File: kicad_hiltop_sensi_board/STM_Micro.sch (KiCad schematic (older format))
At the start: 21 parts, among them SW1 SW_Push, U22 STM32F072RBTx, Y2 8MHZ, Y3 ABS25-32.768KHZ-6-T

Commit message: revb design updated schematics and layout
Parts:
- added C84: 100nF, Capacitor_SMD:C_0402_1005Metric, symbol device:C
- added J9: Conn_02x05_Odd_Even, Connector_PinHeader_2.54mm:PinHeader_2x05_P2.54mm_Vertical, symbol Connector:Conn_02x05_Odd_Even
- added R163: DNF, Resistor_SMD:R_0603_1608Metric, symbol Sensi_Board-rescue:R-device
- added R164: DNF, Resistor_SMD:R_0402_1005Metric, symbol device:R
- added R39, R40: 100k, Capacitor_SMD:C_0603_1608Metric, symbol device:R
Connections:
- net GPIO5 is gone; now on net SB1: U22.33 (I2S2_WS/SPI2_NSS/TIM15_BKIN/TIM1_BKIN/TSC_G6_IO2/USART3_CK/PB12)
- net +3V3: now also C84.2, J9.1 (Pin_1), R39.1
- net ADC7: now also U22.21 (ADC_IN5/CEC/COMP1_INM/COMP2_INM/DAC_OUT2/I2S1_CK/SPI1_SCK/TIM2_CH1/TIM2_ETR/TSC_G2_IO2/PA5); no longer U22.27 (ADC_IN9/TIM14_CH1/TIM1_CH3N/TIM3_CH4/TSC_G3_IO3/USART3_DE/USART3_RTS/PB1)
- net BOOT0: now also R163.1
- net GND: now also C84.1, J9.3 (Pin_3), J9.5 (Pin_5), J9.9 (Pin_9), R163.2, R164.2, R40.1; no longer U22.18 (VSS)
- net NRST: now also J9.10 (Pin_10)
- net SB1: no longer U22.2 (PC13/RTC_OUT_ALARM/RTC_OUT_CALIB/RTC_TAMP1/RTC_TS/SYS_WKUP2)
- net SWD_IO: now also J9.2 (Pin_2), R39.2
- net SWD_SCK: now also J9.4 (Pin_4), R40.2
- net at R124.2: now also U22.27 (ADC_IN9/TIM14_CH1/TIM1_CH3N/TIM3_CH4/TSC_G3_IO3/USART3_DE/USART3_RTS/PB1); no longer U22.21 (ADC_IN5/CEC/COMP1_INM/COMP2_INM/DAC_OUT2/I2S1_CK/SPI1_SCK/TIM2_CH1/TIM2_ETR/TSC_G2_IO2/PA5)
- new net: R164.1, U22.18 (VSS)
- no-connect marks 3 -> 7
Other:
- note added: "JTAG Header\n"
- note added: "Note: only for stm32f072 fit 0R to gnd. for 303/302 model DNF\n"
- moved on the sheet: D13, R124

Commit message: revB ready for review
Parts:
- added J10: Conn_01x04, Connector_PinHeader_1.27mm:PinHeader_1x04_P1.27mm_Vertical, symbol Connector:Conn_01x04
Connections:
- net +3V3: now also J10.1 (Pin_1)
- net DEBUG_UART_RX: now also J10.2 (Pin_2)
- net DEBUG_UART_TX: now also J10.3 (Pin_3)
- net GND: now also J10.4 (Pin_4)
- net SB1 renamed GPIO5
- net SB2 renamed GPIO6
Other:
- note added: "Serial Debug Header\n"
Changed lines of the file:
@@
 STM_RES1
 Text HLabel 11800 3175 2    60   BiDi ~ 0
-SB2
+GPIO6
 Text HLabel 11775 6075 2    60   BiDi ~ 0
 RTD3_INT
 Text HLabel 11775 5975 2    60   BiDi ~ 0
-SB1
+GPIO5
 Text HLabel 11800 4575 2    60   BiDi ~ 0
 GPIO1
@@
 Text Label 4350 3075 2    60   ~ 0
 STM_RESET
+Text Notes 10350 7500 0    118  ~ 24
+Serial Debug Header\n
+Wire Notes Line
+	9950 9225 12575 9225
+Wire Notes Line
+	12575 9225 12575 7250
+Wire Notes Line
+	12575 7250 9950 7250
+Wire Notes Line
+	9950 7250 9950 9225
+$Comp
+L Connector:Conn_01x04 J10
+U 1 1 602D0955
+P 11425 8250
+F 0 "J10" H 11505 8242 50  0000 L CNN
+F 1 "Conn_01x04" H 11505 8151 50  0000 L CNN
+F 2 "Connector_PinHeader_1.27mm:PinHeader_1x04_P1.27mm_Vertical" H 11425 8250 50  0001 C CNN
+F 3 "~" H 11425 8250 50  0001 C CNN
+	1    11425 8250
+	1    0    0    -1
+$EndComp
+$Comp
+L power:+3V3 #PWR0264
+U 1 1 602D1336
+P 11125 8075
+F 0 "#PWR0264" H 11125 7925 50  0001 C CNN
+F 1 "+3V3" H 11140 8248 50  0000 C CNN
+F 2 "" H 11125 8075 50  0001 C CNN
+F 3 "" H 11125 8075 50  0001 C CNN
+	1    11125 8075
+	1    0    0    -1
+$EndComp
+Wire Wire Line
+	11225 8150 11125 8150
+Wire Wire Line
+	11125 8150 11125 8075
+Text Label 10825 5775 0    60   ~ 0
+DEBUG_TX
+Text Label 10825 5875 0    60   ~ 0
+DEBUG_RX
+Text Label 10725 8350 0    60   ~ 0
+DEBUG_TX
+Text Label 10725 8250 0    60   ~ 0
+DEBUG_RX
+Wire Wire Line
+	10725 8250 11225 8250
+Wire Wire Line
+	10725 8350 11225 8350
+$Comp
+L power:GND #PWR0265
+U 1 1 60317C84
+P 11150 8550
+F 0 "#PWR0265" H 11150 8300 50  0001 C CNN
+F 1 "GND" H 11155 8377 50  0000 C CNN
+F 2 "" H 11150 8550 50  0001 C CNN
+F 3 "" H 11150 8550 50  0001 C CNN
+	1    11150 8550
+	1    0    0    -1
+$EndComp
+Wire Wire Line
+	11150 8550 11150 8450
+Wire Wire Line
+	11150 8450 11225 8450
 $EndSCHEMATC

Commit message: Sensi Board RevB
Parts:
- added R172: DNF, Resistor_SMD:R_0603_1608Metric, symbol device:R
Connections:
- net +3V3: now also R172.1
- net BOOT0: now also R172.2
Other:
- moved on the sheet: R120
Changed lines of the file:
@@
 L Sensi_Board-rescue:R-device R120
 U 1 1 5F95CC59
-P 2725 2850
-F 0 "R120" H 2795 2896 50  0000 L CNN
-F 1 "10K" H 2795 2805 50  0000 L CNN
-F 2 "Resistor_SMD:R_0603_1608Metric" V 2655 2850 50  0001 C CNN
-F 3 "" H 2725 2850 50  0001 C CNN
-F 4 "101-010" H 0   0   50  0001 C CNN "Devtank"
-	1    2725 2850
-	1    0    0    -1
-$EndComp
-Wire Wire Line
-	2725 3000 2725 3075
-Connection ~ 2725 3075
+P 3250 2850
+F 0 "R120" H 3320 2896 50  0000 L CNN
+F 1 "10K" H 3320 2805 50  0000 L CNN
+F 2 "Resistor_SMD:R_0603_1608Metric" V 3180 2850 50  0001 C CNN
+F 3 "" H 3250 2850 50  0001 C CNN
+F 4 "101-010" H 525 0   50  0001 C CNN "Devtank"
+	1    3250 2850
+	1    0    0    -1
+$EndComp
+Wire Wire Line
+	3250 3000 3250 3075
 $Comp
 L power:+3V3 #PWR0186
 U 1 1 5F95F542
-P 2725 2625
-F 0 "#PWR0186" H 2725 2475 50  0001 C CNN
-F 1 "+3V3" H 2740 2798 50  0000 C CNN
-F 2 "" H 2725 2625 50  0001 C CNN
-F 3 "" H 2725 2625 50  0001 C CNN
-	1    2725 2625
-	1    0    0    -1
-$EndComp
-Wire Wire Line
-	2725 2625 2725 2700
-Wire Wire Line
-	2300 3075 2725 3075
-Text HLabel 2300 3075 0    60   Input ~ 0
+P 3250 2625
+F 0 "#PWR0186" H 3250 2475 50  0001 C CNN
+F 1 "+3V3" H 3265 2798 50  0000 C CNN
+F 2 "" H 3250 2625 50  0001 C CNN
+F 3 "" H 3250 2625 50  0001 C CNN
+	1    3250 2625
+	1    0    0    -1
+$EndComp
+Wire Wire Line
+	3250 2625 3250 2700
+Wire Wire Line
+	2825 3075 3250 3075
+Text HLabel 2825 3075 0    60   Input ~ 0
 NRST
 Text HLabel 2125 3275 0    60   Input ~ 0
@@
 Wire Wire Line
 	3425 3375 3425 3075
-Connection ~ 3425 3075
-Wire Wire Line
-	3425 3075 2725 3075
 Wire Wire Line
 	3225 6275 3225 6400
@@
 RTD4_CS
 Wire Wire Line
-	2125 3275 2425 3275
+	2125 3275 2300 3275
 Text HLabel 11800 5075 2    60   Input ~ 0
 STM_SPI1_SCK
@@
 Wire Wire Line
 	11150 8450 11225 8450
+Wire Wire Line
+	3425 3075 3250 3075
+Connection ~ 3425 3075
+Connection ~ 3250 3075
+$Comp
+L device:R R172
+U 1 1 603E68CA
+P 2300 3125
+F 0 "R172" H 2370 3171 50  0000 L CNN
+F 1 "DNF" H 2370 3080 50  0000 L CNN
+F 2 "Resistor_SMD:R_0603_1608Metric" V 2230 3125 50  0001 C CNN
+F 3 "" H 2300 3125 50  0001 C CNN
+	1    2300 3125
+	1    0    0    -1
+$EndComp
+Connection ~ 2300 3275
+Wire Wire Line
+	2300 3275 2425 3275
+$Comp
+L power:+3V3 #PWR0266
+U 1 1 603E745A
+P 2300 2925
+F 0 "#PWR0266" H 2300 2775 50  0001 C CNN
+F 1 "+3V3" H 2315 3098 50  0000 C CNN
+F 2 "" H 2300 2925 50  0001 C CNN
+F 3 "" H 2300 2925 50  0001 C CNN
+	1    2300 2925
+	1    0    0    -1
+$EndComp
+Wire Wire Line
+	2300 2975 2300 2925
 $EndSCHEMATC

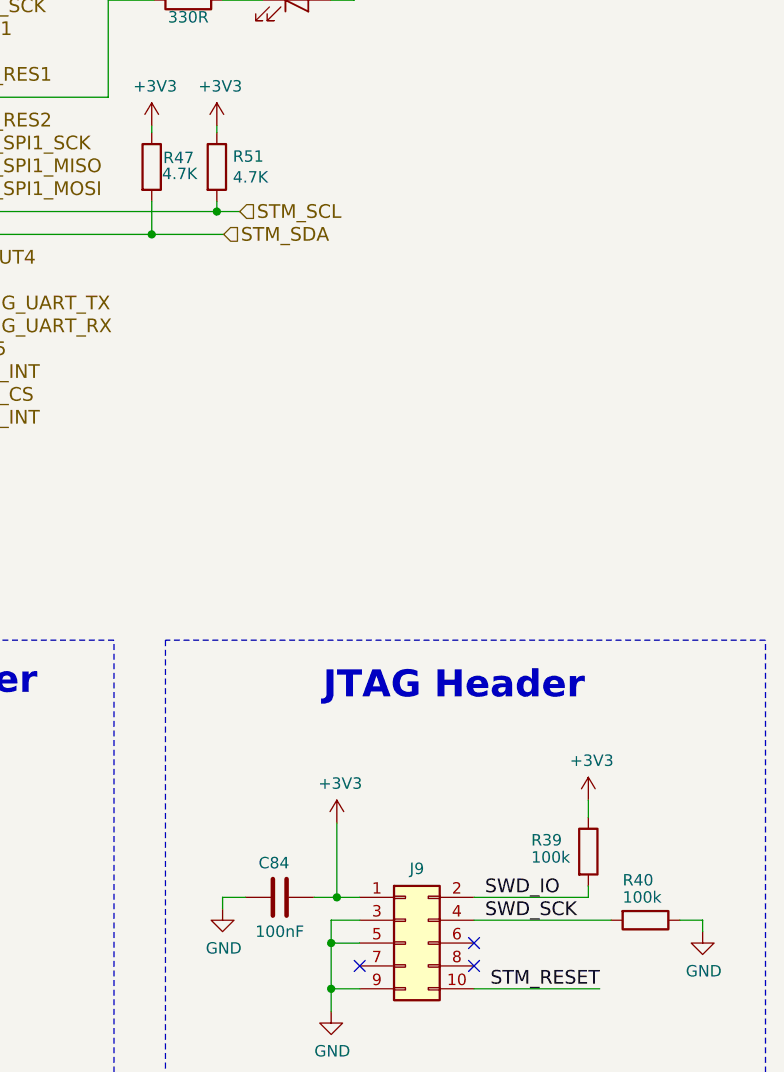
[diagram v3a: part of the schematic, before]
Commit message: updated footprints to simplify bom
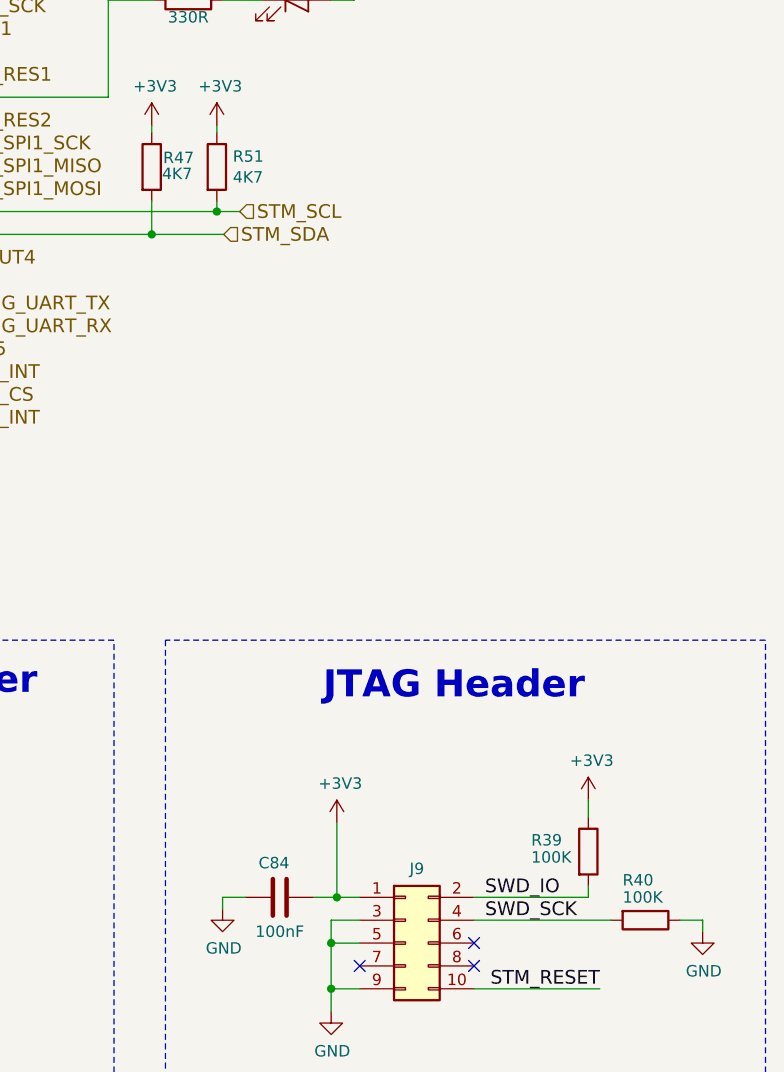
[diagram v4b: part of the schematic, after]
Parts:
- R39, R40: value 100k -> 100K; footprint Capacitor_SMD:C_0603_1608Metric -> Resistor_SMD:R_0603_1608Metric; Devtank (none) -> 101-015
- R47, R51: value 4.7K -> 4K7
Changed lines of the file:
@@
 P 13025 5180
 F 0 "R51" H 13095 5226 50  0000 L CNN
-F 1 "4.7K" H 13095 5135 50  0000 L CNN
+F 1 "4K7" H 13095 5135 50  0000 L CNN
 F 2 "Resistor_SMD:R_0603_1608Metric" V 12955 5180 50  0001 C CNN
 F 3 "" H 13025 5180 50  0001 C CNN
@@
 P 12740 5180
 F 0 "R47" H 12790 5220 50  0000 L CNN
-F 1 "4.7K" H 12785 5150 50  0000 L CNN
+F 1 "4K7" H 12785 5150 50  0000 L CNN
 F 2 "Resistor_SMD:R_0603_1608Metric" V 12670 5180 50  0001 C CNN
 F 3 "" H 12740 5180 50  0001 C CNN
@@
 AR Path="/5F956DB7/6217CF81" Ref="R39"  Part="1"
 F 0 "R39" H 14400 8225 50  0000 L CNN
-F 1 "100k" H 14400 8150 50  0000 L CNN
-F 2 "Capacitor_SMD:C_0603_1608Metric" V 14580 8175 50  0001 C CNN
+F 1 "100K" H 14400 8150 50  0000 L CNN
+F 2 "Resistor_SMD:R_0603_1608Metric" V 14580 8175 50  0001 C CNN
 F 3 "" H 14650 8175 50  0001 C CNN
+F 4 "101-015" H 14650 8175 50  0001 C CNN "Devtank"
 	1    14650 8175
 	1    0    0    -1
@@
 AR Path="/5F956DB7/6217CFAF" Ref="R40"  Part="1"
 F 0 "R40" V 14725 8375 50  0000 L CNN
-F 1 "100k" V 14800 8375 50  0000 L CNN
-F 2 "Capacitor_SMD:C_0603_1608Metric" V 14830 8475 50  0001 C CNN
+F 1 "100K" V 14800 8375 50  0000 L CNN
+F 2 "Resistor_SMD:R_0603_1608Metric" V 14830 8475 50  0001 C CNN
 F 3 "" H 14900 8475 50  0001 C CNN
+F 4 "101-015" H 14900 8475 50  0001 C CNN "Devtank"
 	1    14900 8475
 	0    1    1    0
